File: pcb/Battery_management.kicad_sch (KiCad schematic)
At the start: 16 parts, among them Q1 YJQ3400, Q2 UT6MA2TCR, U10 MCP73831-2-OT, U11 BQ297xy

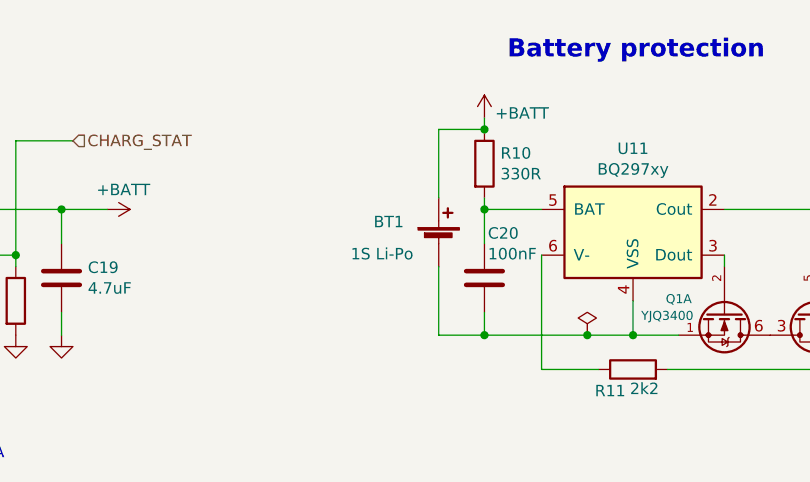
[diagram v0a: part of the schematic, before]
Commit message: PCB: add connection of connector mounting point to ground
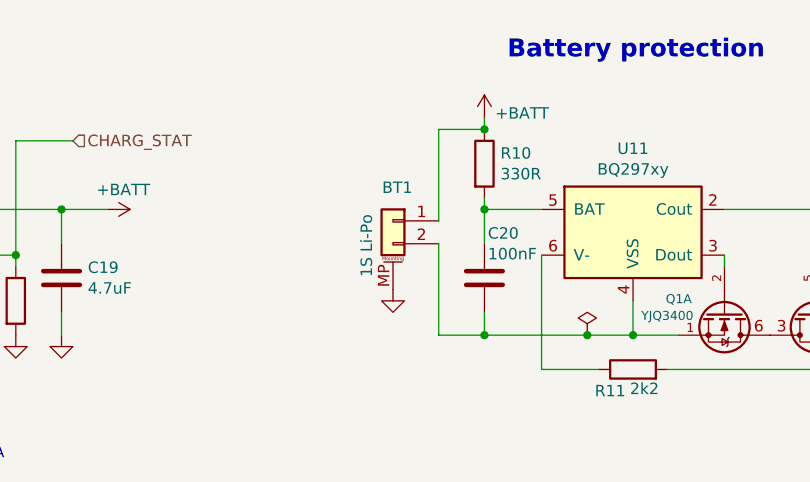
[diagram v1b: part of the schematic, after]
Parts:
- BT1: symbol Device:Battery_Cell -> Connector_Generic_MountingPin:Conn_01x02_MountingPin
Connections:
- net GND: now also BT1.MP (MountPin)
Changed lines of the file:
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@@
     (stroke (width 0) (type solid) (color 0 0 0 0))
   )
-  (wire (pts (xy 151.13 78.74) (xy 151.13 86.36))
+  (wire (pts (xy 151.13 78.74) (xy 151.13 88.9))
     (stroke (width 0) (type solid) (color 0 0 0 0))
   )
@@
     (stroke (width 0) (type solid) (color 0 0 0 0))
   )
-  (wire (pts (xy 151.13 93.98) (xy 151.13 101.6))
+  (wire (pts (xy 151.13 91.44) (xy 151.13 101.6))
     (stroke (width 0) (type solid) (color 0 0 0 0))
   )
@@
     )
     (property "Datasheet" "" (id 3) (at 109.22 101.6 0)
+      (effects (font (size 1.27 1.27)) hide)
+    )
+  )
+  (symbol (lib_id "power:GND") (at 146.05 96.52 0) (unit 1)
+    (in_bom yes) (on_board yes)
+    (property "Reference" "#PWR0199" (id 0) (at 146.05 102.87 0)
+      (effects (font (size 1.27 1.27)) hide)
+    )
+    (property "Value" "GND" (id 1) (at 149.974 98.304 0)
+      (effects (font (size 1.27 1.27)) hide)
+    )
+    (property "Footprint" "" (id 2) (at 146.05 96.52 0)
+      (effects (font (size 1.27 1.27)) hide)
+    )
+    (property "Datasheet" "" (id 3) (at 146.05 96.52 0)
       (effects (font (size 1.27 1.27)) hide)
     )
@@
     )
   )
-  (symbol (lib_id "Device:Battery_Cell") (at 151.13 91.44 0) (unit 1)
-    (in_bom yes) (on_board yes)
-    (property "Reference" "BT1" (id 0) (at 143.8911 89.0206 0)
-      (effects (font (size 1.27 1.27)) (justify left))
-    )
-    (property "Value" "1S Li-Po" (id 1) (at 141.351 92.589 0)
-      (effects (font (size 1.27 1.27)) (justify left))
-    )
-    (property "Footprint" "TCY_connectors:Amphenol_10114830-11102LF_1x02_P1.25mm_Horizontal" (id 2) (at 151.13 89.916 90)
-      (effects (font (size 1.27 1.27)) hide)
-    )
-    (property "Datasheet" "~" (id 3) (at 151.13 89.916 90)
-      (effects (font (size 1.27 1.27)) hide)
-    )
-  )
   (symbol (lib_id "Device:C") (at 156.21 95.25 0) (unit 1)
     (in_bom yes) (on_board yes)
@@
       (effects (font (size 1.27 1.27)) hide)
     )
+  )
+  (symbol (lib_id "Connector_Generic_MountingPin:Conn_01x02_MountingPin") (at 146.05 88.9 0) (mirror y) (unit 1)
+    (in_bom yes) (on_board yes)
+    (property "Reference" "BT1" (id 0) (at 148.2089 85.2106 0)
+      (effects (font (size 1.27 1.27)) (justify left))
+    )
+    (property "Value" "1S Li-Po" (id 1) (at 143.129 95.129 90)
+      (effects (font (size 1.27 1.27)) (justify left))
+    )
+    (property "Footprint" "TCY_connectors:Amphenol_10114830-11102LF_1x02_P1.25mm_Horizontal" (id 2) (at 146.05 87.376 90)
+      (effects (font (size 1.27 1.27)) hide)
+    )
+    (property "Datasheet" "~" (id 3) (at 146.05 87.376 90)
+      (effects (font (size 1.27 1.27)) hide)
+    )

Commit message: Schema & PCB: Update page layout, add notes about SPI modes and I2C addresses
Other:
- company: (none) -> Author: Petr Malaník
- title: (none) -> RingOne
